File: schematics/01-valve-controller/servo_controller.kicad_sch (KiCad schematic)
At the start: 1 part, among them U401 PCA9685PW

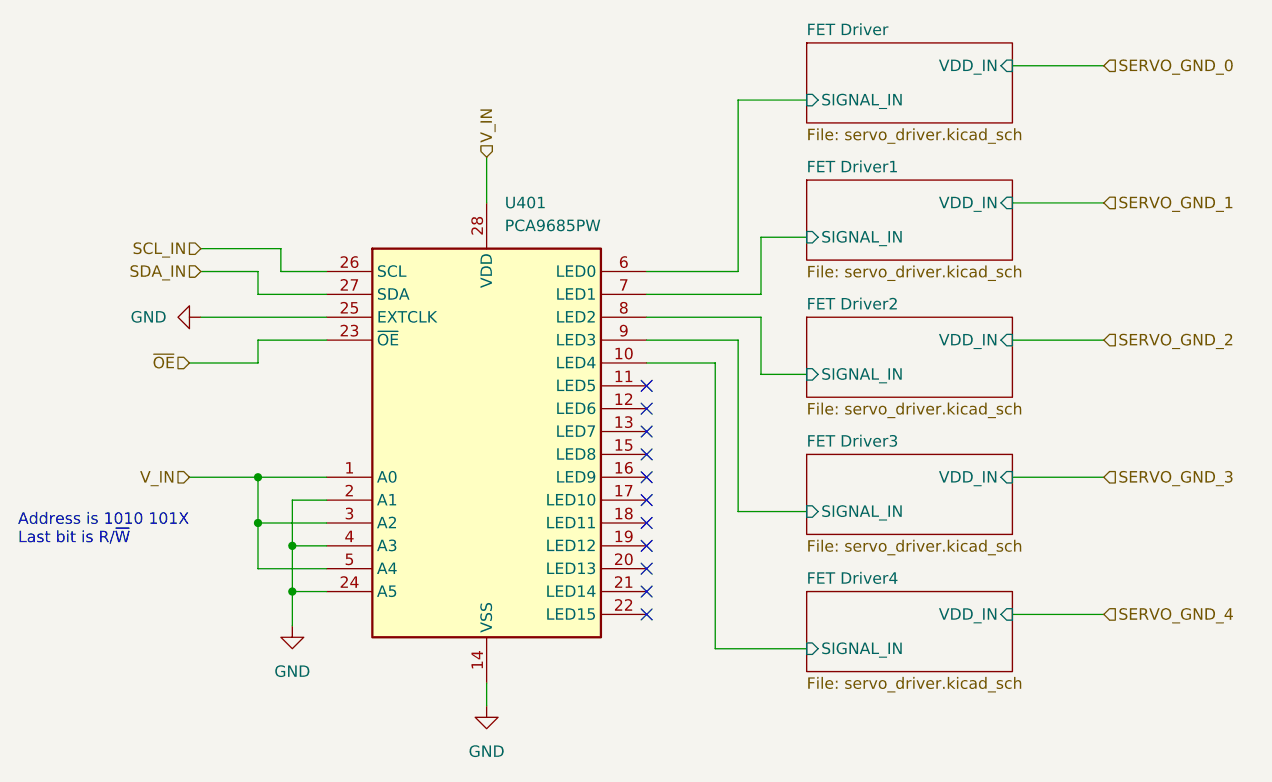
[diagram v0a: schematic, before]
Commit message: Removed driver mosfets
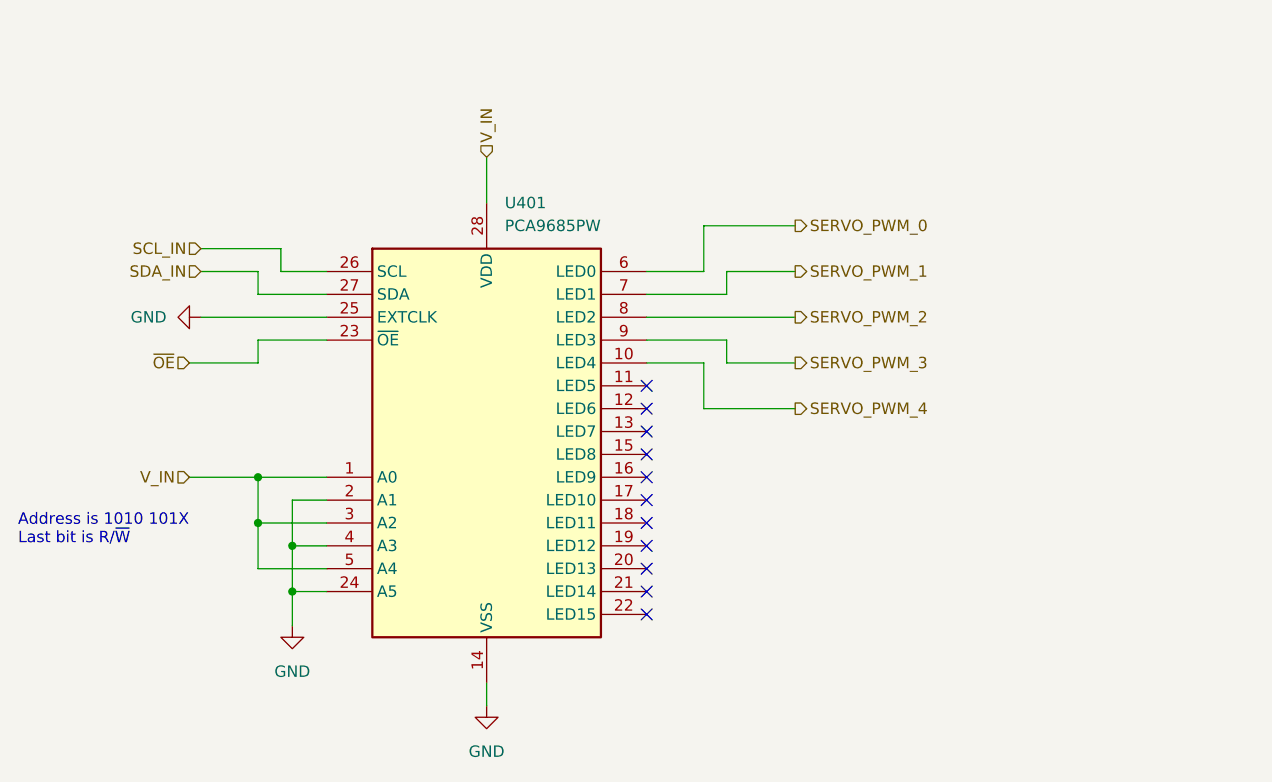
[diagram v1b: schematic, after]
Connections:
- net FET Driver/SIGNAL_IN renamed SERVO_PWM_0
- net FET Driver1/SIGNAL_IN renamed SERVO_PWM_1
- net FET Driver2/SIGNAL_IN renamed SERVO_PWM_2
- net FET Driver3/SIGNAL_IN renamed SERVO_PWM_3
- net FET Driver4/SIGNAL_IN renamed SERVO_PWM_4
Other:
- removed sheet FET Driver
- removed sheet FET Driver1
- removed sheet FET Driver2
- removed sheet FET Driver3
- removed sheet FET Driver4
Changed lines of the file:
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@@
     (stroke (width 0) (type default) (color 0 0 0 0))
   )
-  (wire (pts (xy 148.59 78.74) (xy 148.59 59.69))
-    (stroke (width 0) (type default) (color 0 0 0 0))
-  )
-  (wire (pts (xy 179.07 116.84) (xy 189.23 116.84))
+  (wire (pts (xy 144.78 78.74) (xy 144.78 73.66))
     (stroke (width 0) (type default) (color 0 0 0 0))
   )
@@
     (stroke (width 0) (type default) (color 0 0 0 0))
   )
-  (wire (pts (xy 179.07 86.36) (xy 189.23 86.36))
-    (stroke (width 0) (type default) (color 0 0 0 0))
-  )
   (wire (pts (xy 95.25 88.9) (xy 95.25 86.36))
     (stroke (width 0) (type default) (color 0 0 0 0))
@@
     (stroke (width 0) (type default) (color 0 0 0 0))
   )
-  (wire (pts (xy 151.13 83.82) (xy 151.13 90.17))
-    (stroke (width 0) (type default) (color 0 0 0 0))
-  )
   (wire (pts (xy 99.06 114.3) (xy 99.06 118.11))
     (stroke (width 0) (type default) (color 0 0 0 0))
@@
     (stroke (width 0) (type default) (color 0 0 0 0))
   )
-  (wire (pts (xy 148.59 86.36) (xy 148.59 105.41))
+  (wire (pts (xy 147.32 86.36) (xy 147.32 88.9))
     (stroke (width 0) (type default) (color 0 0 0 0))
   )
@@
     (stroke (width 0) (type default) (color 0 0 0 0))
   )
-  (wire (pts (xy 151.13 90.17) (xy 156.21 90.17))
-    (stroke (width 0) (type default) (color 0 0 0 0))
-  )
   (wire (pts (xy 102.87 106.68) (xy 95.25 106.68))
     (stroke (width 0) (type default) (color 0 0 0 0))
@@
     (stroke (width 0) (type default) (color 0 0 0 0))
   )
-  (wire (pts (xy 146.05 88.9) (xy 146.05 120.65))
-    (stroke (width 0) (type default) (color 0 0 0 0))
-  )
-  (wire (pts (xy 148.59 59.69) (xy 156.21 59.69))
-    (stroke (width 0) (type default) (color 0 0 0 0))
-  )
-  (wire (pts (xy 179.07 55.88) (xy 189.23 55.88))
-    (stroke (width 0) (type default) (color 0 0 0 0))
-  )
-  (wire (pts (xy 179.07 71.12) (xy 189.23 71.12))
-    (stroke (width 0) (type default) (color 0 0 0 0))
-  )
-  (wire (pts (xy 138.43 81.28) (xy 151.13 81.28))
-    (stroke (width 0) (type default) (color 0 0 0 0))
-  )
-  (wire (pts (xy 138.43 88.9) (xy 146.05 88.9))
+  (wire (pts (xy 144.78 88.9) (xy 144.78 93.98))
+    (stroke (width 0) (type default) (color 0 0 0 0))
+  )
+  (wire (pts (xy 144.78 73.66) (xy 154.94 73.66))
+    (stroke (width 0) (type default) (color 0 0 0 0))
+  )
+  (wire (pts (xy 138.43 81.28) (xy 147.32 81.28))
+    (stroke (width 0) (type default) (color 0 0 0 0))
+  )
+  (wire (pts (xy 138.43 88.9) (xy 144.78 88.9))
     (stroke (width 0) (type default) (color 0 0 0 0))
   )
@@
     (stroke (width 0) (type default) (color 0 0 0 0))
   )
-  (wire (pts (xy 179.07 101.6) (xy 189.23 101.6))
-    (stroke (width 0) (type default) (color 0 0 0 0))
-  )
   (wire (pts (xy 88.9 76.2) (xy 97.79 76.2))
     (stroke (width 0) (type default) (color 0 0 0 0))
   )
-  (wire (pts (xy 151.13 74.93) (xy 156.21 74.93))
-    (stroke (width 0) (type default) (color 0 0 0 0))
-  )
-  (wire (pts (xy 138.43 86.36) (xy 148.59 86.36))
+  (wire (pts (xy 147.32 78.74) (xy 154.94 78.74))
+    (stroke (width 0) (type default) (color 0 0 0 0))
+  )
+  (wire (pts (xy 138.43 86.36) (xy 147.32 86.36))
     (stroke (width 0) (type default) (color 0 0 0 0))
   )
@@
     (stroke (width 0) (type default) (color 0 0 0 0))
   )
-  (wire (pts (xy 151.13 81.28) (xy 151.13 74.93))
+  (wire (pts (xy 147.32 81.28) (xy 147.32 78.74))
     (stroke (width 0) (type default) (color 0 0 0 0))
   )
@@
     (stroke (width 0) (type default) (color 0 0 0 0))
   )
-  (wire (pts (xy 146.05 120.65) (xy 156.21 120.65))
-    (stroke (width 0) (type default) (color 0 0 0 0))
-  )
-  (wire (pts (xy 138.43 78.74) (xy 148.59 78.74))
-    (stroke (width 0) (type default) (color 0 0 0 0))
-  )
-  (wire (pts (xy 138.43 83.82) (xy 151.13 83.82))
+  (wire (pts (xy 144.78 93.98) (xy 154.94 93.98))
+    (stroke (width 0) (type default) (color 0 0 0 0))
+  )
+  (wire (pts (xy 138.43 78.74) (xy 144.78 78.74))
+    (stroke (width 0) (type default) (color 0 0 0 0))
+  )
+  (wire (pts (xy 138.43 83.82) (xy 154.94 83.82))
     (stroke (width 0) (type default) (color 0 0 0 0))
   )
@@
     (stroke (width 0) (type default) (color 0 0 0 0))
   )
-  (wire (pts (xy 148.59 105.41) (xy 156.21 105.41))
+  (wire (pts (xy 147.32 88.9) (xy 154.94 88.9))
     (stroke (width 0) (type default) (color 0 0 0 0))
   )
@@
     (effects (font (size 1.27 1.27)) (justify right))
   )
-  (hierarchical_label "SERVO_GND_1" (shape input) (at 189.23 71.12 0)
-    (effects (font (size 1.27 1.27)) (justify left))
-  )
-  (hierarchical_label "SERVO_GND_0" (shape input) (at 189.23 55.88 0)
+  (hierarchical_label "SERVO_PWM_1" (shape output) (at 154.94 78.74 0)
+    (effects (font (size 1.27 1.27)) (justify left))
+  )
+  (hierarchical_label "SERVO_PWM_0" (shape output) (at 154.94 73.66 0)
     (effects (font (size 1.27 1.27)) (justify left))
   )
@@
     (effects (font (size 1.27 1.27)) (justify left))
   )
-  (hierarchical_label "SERVO_GND_4" (shape input) (at 189.23 116.84 0)
+  (hierarchical_label "SERVO_PWM_4" (shape output) (at 154.94 93.98 0)
     (effects (font (size 1.27 1.27)) (justify left))
   )
@@
     (effects (font (size 1.27 1.27)) (justify right))
   )
-  (hierarchical_label "SERVO_GND_2" (shape input) (at 189.23 86.36 0)
-    (effects (font (size 1.27 1.27)) (justify left))
-  )
-  (hierarchical_label "SERVO_GND_3" (shape input) (at 189.23 101.6 0)
+  (hierarchical_label "SERVO_PWM_2" (shape output) (at 154.94 83.82 0)
+    (effects (font (size 1.27 1.27)) (justify left))
+  )
+  (hierarchical_label "SERVO_PWM_3" (shape output) (at 154.94 88.9 0)
     (effects (font (size 1.27 1.27)) (justify left))
   )
@@
     (pin "1")
   )
-  (sheet (at 156.21 83.82) (size 22.86 8.89) (fields_autoplaced)
-    (stroke (width 0.1524) (type solid) (color 0 0 0 0))
-    (fill (color 0 0 0 0.0000))
-    (property "Sheet name" "FET Driver2" (id 0) (at 156.21 83.1084 0)
-      (effects (font (size 1.27 1.27)) (justify left bottom))
-    )
-    (property "Sheet file" "servo_driver.kicad_sch" (id 1) (at 156.21 93.2946 0)
-      (effects (font (size 1.27 1.27)) (justify left top))
-    )
-    (pin "VDD_IN" input (at 179.07 86.36 0)
-      (effects (font (size 1.27 1.27)) (justify right))
-    )
-    (pin "SIGNAL_IN" input (at 156.21 90.17 180)
-      (effects (font (size 1.27 1.27)) (justify left))
-    )
-  )
-  (sheet (at 156.21 114.3) (size 22.86 8.89) (fields_autoplaced)
-    (stroke (width 0.1524) (type solid) (color 0 0 0 0))
-    (fill (color 0 0 0 0.0000))
-    (property "Sheet name" "FET Driver4" (id 0) (at 156.21 113.5884 0)
-      (effects (font (size 1.27 1.27)) (justify left bottom))
-    )
-    (property "Sheet file" "servo_driver.kicad_sch" (id 1) (at 156.21 123.7746 0)
-      (effects (font (size 1.27 1.27)) (justify left top))
-    )
-    (pin "VDD_IN" input (at 179.07 116.84 0)
-      (effects (font (size 1.27 1.27)) (justify right))
-    )
-    (pin "SIGNAL_IN" input (at 156.21 120.65 180)
-      (effects (font (size 1.27 1.27)) (justify left))
-    )
-  )
-  (sheet (at 156.21 68.58) (size 22.86 8.89) (fields_autoplaced)
-    (stroke (width 0.1524) (type solid) (color 0 0 0 0))
-    (fill (color 0 0 0 0.0000))
-    (property "Sheet name" "FET Driver1" (id 0) (at 156.21 67.8684 0)
-      (effects (font (size 1.27 1.27)) (justify left bottom))
-    )
-    (property "Sheet file" "servo_driver.kicad_sch" (id 1) (at 156.21 78.0546 0)
-      (effects (font (size 1.27 1.27)) (justify left top))
-    )
-    (pin "VDD_IN" input (at 179.07 71.12 0)
-      (effects (font (size 1.27 1.27)) (justify right))
-    )
-    (pin "SIGNAL_IN" input (at 156.21 74.93 180)
-      (effects (font (size 1.27 1.27)) (justify left))
-    )
-  )
-  (sheet (at 156.21 53.34) (size 22.86 8.89) (fields_autoplaced)
-    (stroke (width 0.1524) (type solid) (color 0 0 0 0))
-    (fill (color 0 0 0 0.0000))
-    (property "Sheet name" "FET Driver" (id 0) (at 156.21 52.6284 0)
-      (effects (font (size 1.27 1.27)) (justify left bottom))
-    )
-    (property "Sheet file" "servo_driver.kicad_sch" (id 1) (at 156.21 62.8146 0)
-      (effects (font (size 1.27 1.27)) (justify left top))
-    )
-    (pin "VDD_IN" input (at 179.07 55.88 0)
-      (effects (font (size 1.27 1.27)) (justify right))
-    )
-    (pin "SIGNAL_IN" input (at 156.21 59.69 180)
-      (effects (font (size 1.27 1.27)) (justify left))
-    )
-  )
-  (sheet (at 156.21 99.06) (size 22.86 8.89) (fields_autoplaced)
-    (stroke (width 0.1524) (type solid) (color 0 0 0 0))
-    (fill (color 0 0 0 0.0000))
-    (property "Sheet name" "FET Driver3" (id 0) (at 156.21 98.3484 0)
-      (effects (font (size 1.27 1.27)) (justify left bottom))
-    )
-    (property "Sheet file" "servo_driver.kicad_sch" (id 1) (at 156.21 108.5346 0)
-      (effects (font (size 1.27 1.27)) (justify left top))
-    )
-    (pin "VDD_IN" input (at 179.07 101.6 0)
-      (effects (font (size 1.27 1.27)) (justify right))
-    )
-    (pin "SIGNAL_IN" input (at 156.21 105.41 180)
-      (effects (font (size 1.27 1.27)) (justify left))
-    )
-  )
   (sheet_instances

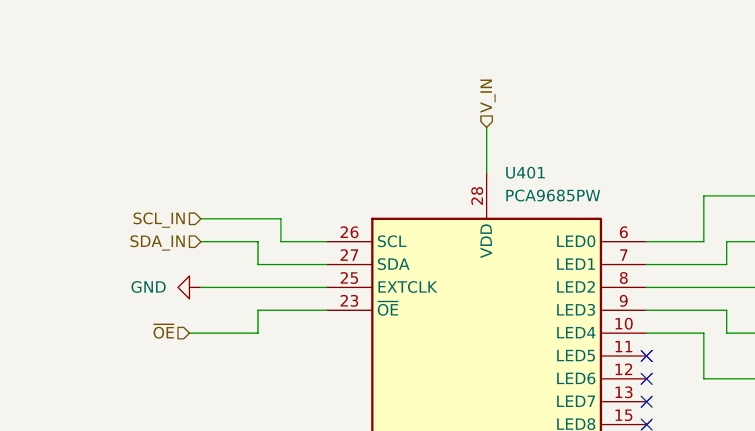
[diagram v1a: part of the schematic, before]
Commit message: DC output switching, GPIO expander
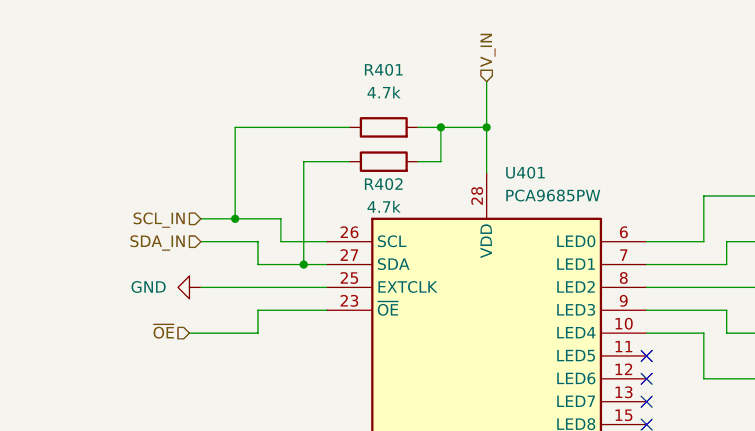
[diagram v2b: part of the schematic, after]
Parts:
- added R401, R402: 4.7k, symbol Device:R
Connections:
- net SCL_IN: now also R401.1
- net SDA_IN: now also R402.1
- net V_IN: now also R401.2, R402.2
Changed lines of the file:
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@@
   (junction (at 95.25 106.68) (diameter 0) (color 0 0 0 0)
   )
+  (junction (at 115.57 66.04) (diameter 0) (color 0 0 0 0)
+  )
   (junction (at 99.06 114.3) (diameter 0) (color 0 0 0 0)
   )
   (junction (at 99.06 109.22) (diameter 0) (color 0 0 0 0)
   )
+  (junction (at 100.33 81.28) (diameter 0) (color 0 0 0 0)
+  )
+  (junction (at 92.71 76.2) (diameter 0) (color 0 0 0 0)
+  )
   (junction (at 95.25 101.6) (diameter 0) (color 0 0 0 0)
+  )
+  (junction (at 120.65 66.04) (diameter 0) (color 0 0 0 0)
   )
   (no_connect (at 138.43 111.76))
@@
     (stroke (width 0) (type default) (color 0 0 0 0))
   )
+  (wire (pts (xy 92.71 66.04) (xy 92.71 76.2))
+    (stroke (width 0) (type default) (color 0 0 0 0))
+  )
   (wire (pts (xy 144.78 78.74) (xy 144.78 73.66))
     (stroke (width 0) (type default) (color 0 0 0 0))
@@
     (stroke (width 0) (type default) (color 0 0 0 0))
   )
+  (wire (pts (xy 113.03 69.85) (xy 115.57 69.85))
+    (stroke (width 0) (type default) (color 0 0 0 0))
+  )
   (wire (pts (xy 95.25 101.6) (xy 102.87 101.6))
     (stroke (width 0) (type default) (color 0 0 0 0))
   )
+  (wire (pts (xy 120.65 66.04) (xy 120.65 71.12))
+    (stroke (width 0) (type default) (color 0 0 0 0))
+  )
   (wire (pts (xy 95.25 88.9) (xy 95.25 86.36))
     (stroke (width 0) (type default) (color 0 0 0 0))
@@
     (stroke (width 0) (type default) (color 0 0 0 0))
   )
+  (wire (pts (xy 95.25 81.28) (xy 100.33 81.28))
+    (stroke (width 0) (type default) (color 0 0 0 0))
+  )
   (wire (pts (xy 99.06 114.3) (xy 99.06 118.11))
     (stroke (width 0) (type default) (color 0 0 0 0))
@@
     (stroke (width 0) (type default) (color 0 0 0 0))
   )
-  (wire (pts (xy 120.65 66.04) (xy 120.65 71.12))
+  (wire (pts (xy 92.71 66.04) (xy 105.41 66.04))
+    (stroke (width 0) (type default) (color 0 0 0 0))
+  )
+  (wire (pts (xy 120.65 60.96) (xy 120.65 66.04))
     (stroke (width 0) (type default) (color 0 0 0 0))
   )
@@
     (stroke (width 0) (type default) (color 0 0 0 0))
   )
+  (wire (pts (xy 115.57 66.04) (xy 120.65 66.04))
+    (stroke (width 0) (type default) (color 0 0 0 0))
+  )
+  (wire (pts (xy 113.03 66.04) (xy 115.57 66.04))
+    (stroke (width 0) (type default) (color 0 0 0 0))
+  )
   (wire (pts (xy 102.87 106.68) (xy 95.25 106.68))
     (stroke (width 0) (type default) (color 0 0 0 0))
   )
-  (wire (pts (xy 95.25 81.28) (xy 102.87 81.28))
-    (stroke (width 0) (type default) (color 0 0 0 0))
-  )
   (wire (pts (xy 144.78 88.9) (xy 144.78 93.98))
     (stroke (width 0) (type default) (color 0 0 0 0))
@@
     (stroke (width 0) (type default) (color 0 0 0 0))
   )
+  (wire (pts (xy 115.57 66.04) (xy 115.57 69.85))
+    (stroke (width 0) (type default) (color 0 0 0 0))
+  )
   (wire (pts (xy 138.43 81.28) (xy 147.32 81.28))
     (stroke (width 0) (type default) (color 0 0 0 0))
@@
     (stroke (width 0) (type default) (color 0 0 0 0))
   )
+  (wire (pts (xy 100.33 81.28) (xy 102.87 81.28))
+    (stroke (width 0) (type default) (color 0 0 0 0))
+  )
   (wire (pts (xy 99.06 109.22) (xy 102.87 109.22))
     (stroke (width 0) (type default) (color 0 0 0 0))
   )
+  (wire (pts (xy 100.33 69.85) (xy 100.33 81.28))
+    (stroke (width 0) (type default) (color 0 0 0 0))
+  )
   (wire (pts (xy 120.65 124.46) (xy 120.65 127))
     (stroke (width 0) (type default) (color 0 0 0 0))
   )
-  (wire (pts (xy 88.9 76.2) (xy 97.79 76.2))
+  (wire (pts (xy 105.41 69.85) (xy 100.33 69.85))
+    (stroke (width 0) (type default) (color 0 0 0 0))
+  )
+  (wire (pts (xy 88.9 76.2) (xy 92.71 76.2))
     (stroke (width 0) (type default) (color 0 0 0 0))
   )
@@
   )
   (wire (pts (xy 138.43 78.74) (xy 144.78 78.74))
+    (stroke (width 0) (type default) (color 0 0 0 0))
+  )
+  (wire (pts (xy 92.71 76.2) (xy 97.79 76.2))
     (stroke (width 0) (type default) (color 0 0 0 0))
   )
@@
     (effects (font (size 1.27 1.27)) (justify left))
   )
-  (hierarchical_label "V_IN" (shape input) (at 120.65 66.04 90)
+  (hierarchical_label "V_IN" (shape input) (at 120.65 60.96 90)
     (effects (font (size 1.27 1.27)) (justify left))
   )
@@
     (pin "1")
   )
+  (symbol (lib_id "Device:R") (at 109.22 69.85 90) (unit 1)
+    (in_bom yes) (on_board yes)
+    (property "Reference" "R402" (id 0) (at 109.22 72.39 90))
+    (property "Value" "4.7k" (id 1) (at 109.22 74.93 90))
+    (property "Footprint" "" (id 2) (at 109.22 71.628 90)
+      (effects (font (size 1.27 1.27)) hide)
+    )
+    (property "Datasheet" "~" (id 3) (at 109.22 69.85 0)
+      (effects (font (size 1.27 1.27)) hide)
+    )
+    (pin "1")
+    (pin "2")
+  )
   (symbol (lib_id "power:GND") (at 88.9 83.82 270) (unit 1)
     (in_bom yes) (on_board yes) (fields_autoplaced)
@@
     (pin "1")
   )
+  (symbol (lib_id "Device:R") (at 109.22 66.04 90) (unit 1)
+    (in_bom yes) (on_board yes) (fields_autoplaced)
+    (property "Reference" "R401" (id 0) (at 109.22 59.69 90))
+    (property "Value" "4.7k" (id 1) (at 109.22 62.23 90))
+    (property "Footprint" "" (id 2) (at 109.22 67.818 90)
+      (effects (font (size 1.27 1.27)) hide)
+    )
+    (property "Datasheet" "~" (id 3) (at 109.22 66.04 0)
+      (effects (font (size 1.27 1.27)) hide)
+    )
+    (pin "1")
+    (pin "2")
+  )
   (sheet_instances
